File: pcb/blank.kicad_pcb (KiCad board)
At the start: 2 copper layers, 104.8 x 90.6 mm, 0 parts

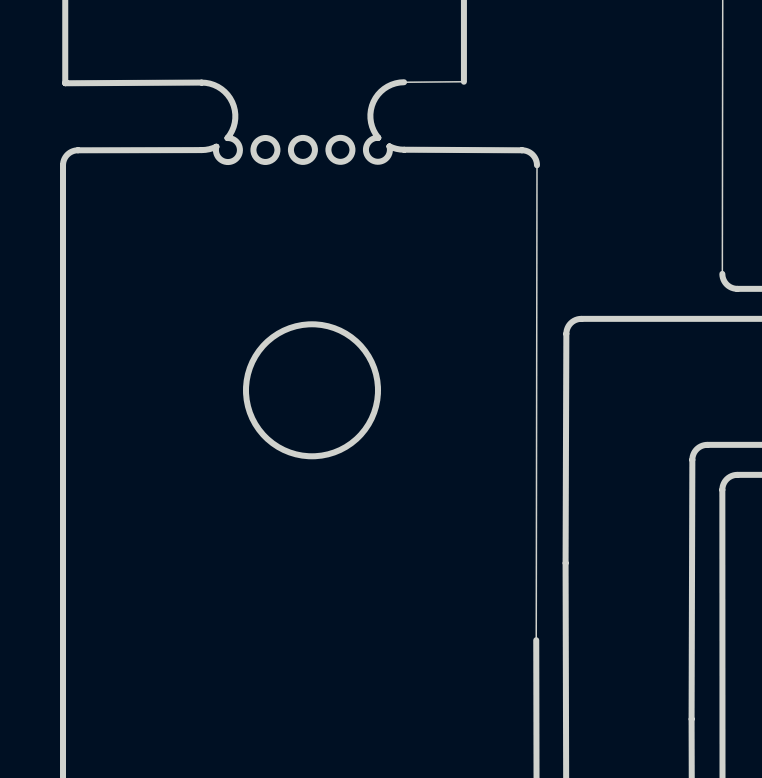
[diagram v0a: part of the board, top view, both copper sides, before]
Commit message: Add new backup files and initial configuration for PCB project
- Added two new backup zip files: flex-2026-06-25_022102.zip and flex-2026-06-25_025018.zip.
- Created fp-info-cache file with initial content.
- Established fp-lib-table with custom library configuration.
- Introduced new PCB layout file: sweep.kicad_pcb.
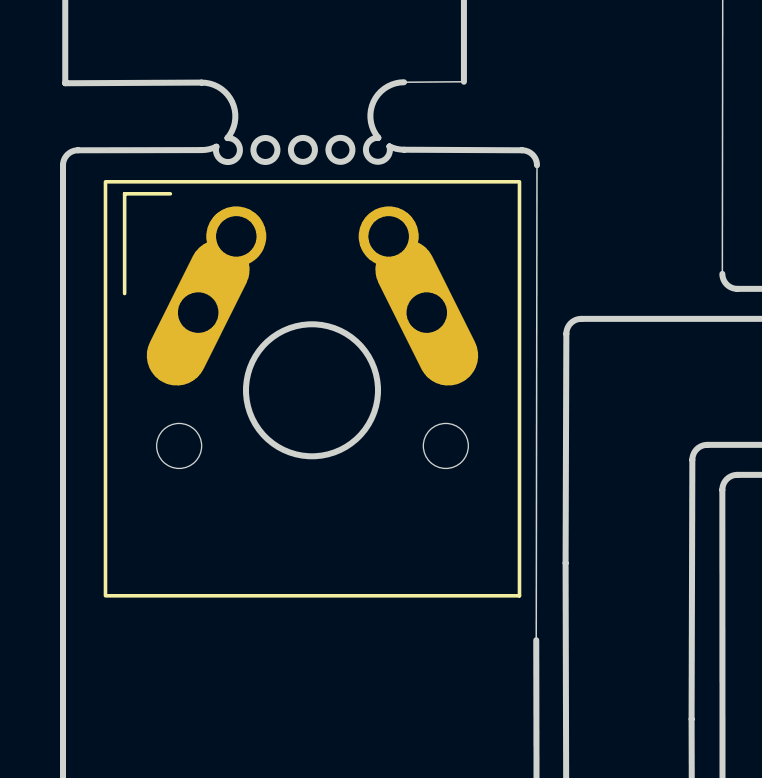
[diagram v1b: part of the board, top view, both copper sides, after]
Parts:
- added SW6: SW_Push, custom:SW_Choc_reversible, B.Cu at (65.2, 78.2)
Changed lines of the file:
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@@
   (gr_circle (center 64.923003 70.271903) (end 65.323003 70.271903) (layer "Edge.Cuts") (width 0.2) (fill none))
   (gr_circle (center 108.817995 56.02811) (end 109.217995 56.02811) (layer "Edge.Cuts") (width 0.2) (fill none))
+  (footprint "custom:SW_Choc_reversible" (layer "B.Cu")
+    (at 65.241599 78.2348 180)
+    (descr "Choc V2 (PG1232/CPG1232) low-profile keyswitch, reversible for top/bottom mount")
+    (tags "Choc V2 PG1232 CPG1232 Kailh low-profile reversible")
+    (attr through_hole)
+    (fp_text reference "SW6" (at 0 8.255) (layer "B.SilkS") hide
+      (effects (font (size 1 1) (thickness 0.15)) (justify mirror))
 )
+    (fp_text value "SW_Push" (at 0 -8.255) (layer "B.Fab")
+      (effects (font (size 1 1) (thickness 0.15)) (justify mirror))
+)
+    (fp_text user "${REFERENCE}" (at 0 8.255) (layer "F.SilkS") hide
+      (effects (font (size 1 1) (thickness 0.15)))
+)
+    (fp_text user "${REFERENCE}" (at 0 0) (layer "B.Fab")
+      (effects (font (size 1 1) (thickness 0.15)) (justify mirror))
+)
+    (fp_text user "${VALUE}" (at 0 -8.255) (layer "F.Fab")
+      (effects (font (size 1 1) (thickness 0.15)))
+)
+    (fp_text user "${REFERENCE}" (at 0 0) (layer "F.Fab")
+      (effects (font (size 1 1) (thickness 0.15)))
+)
+    (fp_rect (start -7 -7) (end 7 7) (stroke (width 0.15) (type default)) (fill none) (layer "F.Fab"))
+    (fp_rect (start -7 -7) (end 7 7) (stroke (width 0.15) (type default)) (fill none) (layer "B.Fab"))
+    (fp_rect (start -6.9 -6.9) (end 6.9 6.9) (stroke (width 0.12) (type default)) (fill none) (layer "F.SilkS"))
+    (fp_rect (start -6.9 -6.9) (end 6.9 6.9) (stroke (width 0.12) (type default)) (fill none) (layer "B.SilkS"))
+    (fp_rect (start -7.5 -7.5) (end 7.5 7.5) (stroke (width 0.05) (type default)) (fill none) (layer "F.CrtYd"))
+    (fp_line (start -6.15 6.498) (end -6.15 3.173) (layer "B.SilkS") (width 0.12))
+    (fp_line (start -6.15 6.498) (end -4.625 6.498) (layer "B.SilkS") (width 0.12))
+    (fp_line (start 6.2625 6.5) (end 6.2625 3.175) (layer "F.SilkS") (width 0.12))
+    (fp_line (start 6.2625 6.5) (end 4.7375 6.5) (layer "F.SilkS") (width 0.12))
+    (pad "" np_thru_hole circle (at -4.445 -1.905) (size 1.5 1.5) (drill 1.5) (layers "*.Cu" "*.Mask"))
+    (pad "" np_thru_hole circle (at 4.445 -1.905) (size 1.5 1.5) (drill 1.5) (layers "*.Cu" "*.Mask"))
+    (pad "1" thru_hole circle (at -2.54 5.08 180) (size 2 2) (drill 1.35) (layers "*.Cu" "*.Mask"))
+    (pad "1" thru_hole oval (at -3.81 2.54 206.5) (size 2 5.2) (drill 1.35) (layers "*.Cu" "*.Mask"))
+    (pad "2" thru_hole circle (at 2.54 5.08 180) (size 2 2) (drill 1.35) (layers "*.Cu" "*.Mask"))
+    (pad "2" thru_hole oval (at 3.81 2.54 153.5) (size 2 5.2) (drill 1.35) (layers "*.Cu" "*.Mask"))
+  )
+)
